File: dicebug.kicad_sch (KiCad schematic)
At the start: 39 parts, among them SW1 SW_SPDT, U1 74LV163ADR, U3 74HCS7266DR, U5 iqs211b

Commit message: schematic: added license info
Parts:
- R8: value 47k -> 51k
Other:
- company: Till Straumann -> Till Straumann; Artwork by Adam.
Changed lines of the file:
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@@
     (date "2023-05-30")
     (rev "1.0")
-    (company "Till Straumann")
+    (company "Till Straumann; Artwork by Adam.")
+    (comment 1 "License: OHL-S/CC-BY-NC-ND")
   )
   (junction (at 231.14 71.755) (diameter 0) (color 0 0 0 0)
@@
       (effects (font (size 1.27 1.27)) (justify left))
     )
-    (property "Value" "47k" (at 81.5086 62.103 0)
-      (effects (font (size 1.27 1.27)) (justify left))
-    )
+    (property "Value" "51k" (at 81.5086 62.103 0)
+      (effects (font (size 1.27 1.27)) (justify left))
+    )

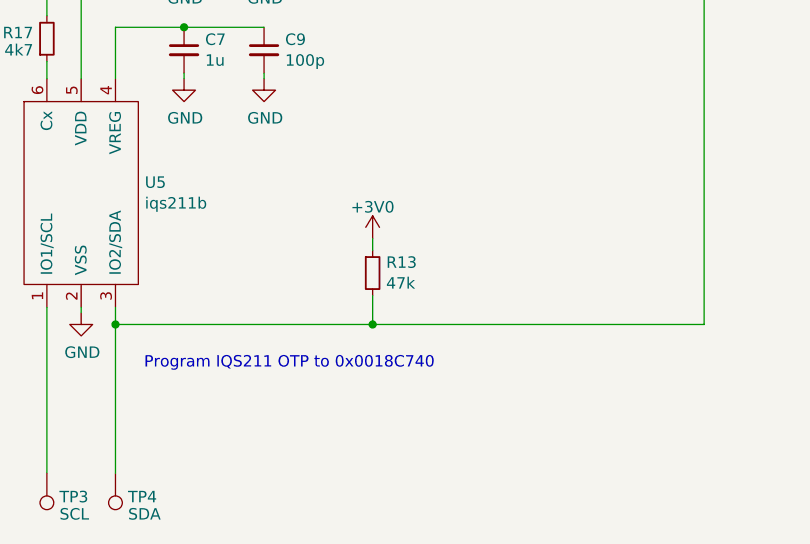
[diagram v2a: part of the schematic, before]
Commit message: Changed second resistor from 47k to 51k
The reason for using 51k is simply for easier identification.
If the resistors have their values printed on the package
you can distinguish 4k7 vs 51k simply by looking for a 4 vs 5...
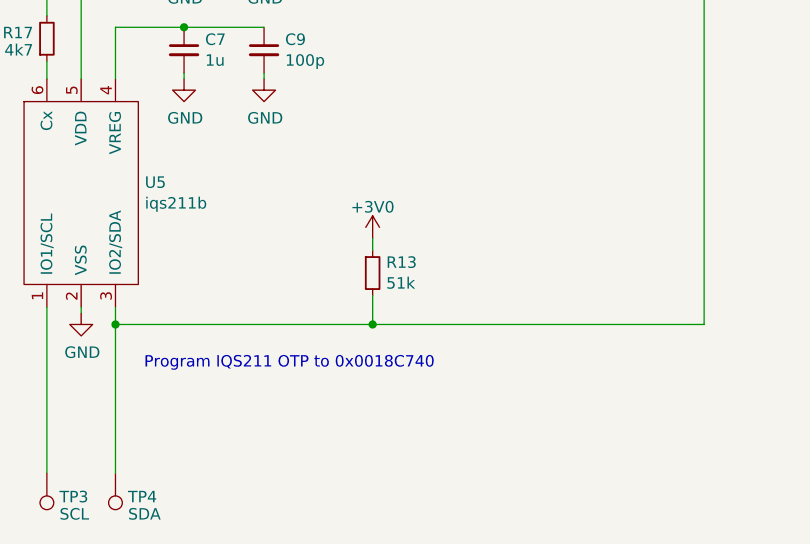
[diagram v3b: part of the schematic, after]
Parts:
- R13: value 47k -> 51k
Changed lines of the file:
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@@
       (effects (font (size 1.27 1.27)) (justify left))
     )
-    (property "Value" "47k" (at 103.0986 152.908 0)
+    (property "Value" "51k" (at 103.0986 152.908 0)
       (effects (font (size 1.27 1.27)) (justify left))
     )
